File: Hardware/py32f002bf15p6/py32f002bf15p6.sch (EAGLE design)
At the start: 26 parts, among them IC1 PY32F002BF15P6TU, IC2 AP2114HA-3.3TRG1, J1 USB_MINI-B_SMT, Y1 DSC6083CI1A-350K000T

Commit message: Replaced 4.7uf 0805 caps for larger 1206 parts
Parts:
- C10, C9: device rcl:C-EUC0805 -> rcl:C-EUC1206
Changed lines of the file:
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@@
 <part name="GND17" library="supply1" library_urn="urn:adsk.eagle:library:371" deviceset="GND" device=""/>
 <part name="GND19" library="supply1" library_urn="urn:adsk.eagle:library:371" deviceset="GND" device=""/>
-<part name="C9" library="rcl" library_urn="urn:adsk.eagle:library:334" deviceset="C-EU" device="C0805" package3d_urn="urn:adsk.eagle:package:23617/2" value="4.7uf"/>
+<part name="C9" library="rcl" library_urn="urn:adsk.eagle:library:334" deviceset="C-EU" device="C1206" package3d_urn="urn:adsk.eagle:package:23618/2" value="4.7uf"/>
 <part name="GND20" library="supply1" library_urn="urn:adsk.eagle:library:371" deviceset="GND" device=""/>
-<part name="C10" library="rcl" library_urn="urn:adsk.eagle:library:334" deviceset="C-EU" device="C0805" package3d_urn="urn:adsk.eagle:package:23617/2" value="4.7uf"/>
+<part name="C10" library="rcl" library_urn="urn:adsk.eagle:library:334" deviceset="C-EU" device="C1206" package3d_urn="urn:adsk.eagle:package:23618/2" value="4.7uf"/>
 <part name="GND21" library="supply1" library_urn="urn:adsk.eagle:library:371" deviceset="GND" device=""/>
 <part name="+3V9" library="supply1" library_urn="urn:adsk.eagle:library:371" deviceset="+3V3" device=""/>

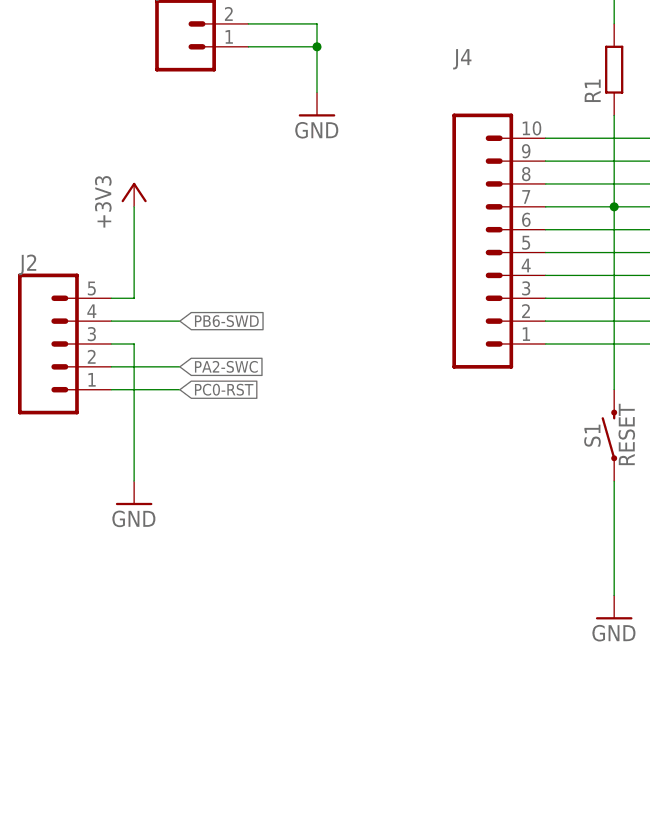
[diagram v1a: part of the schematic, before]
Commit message: Updated silkscreen, removed reset header pin
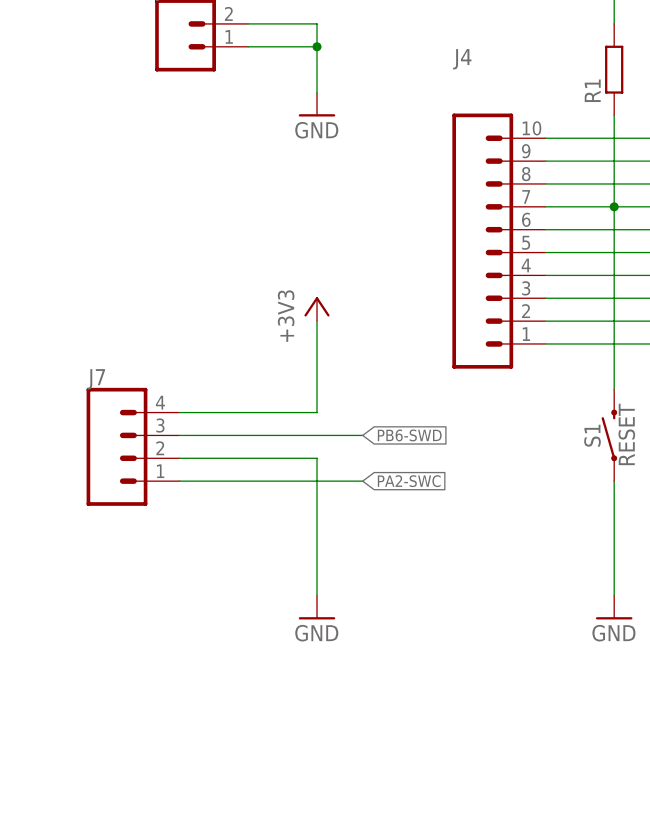
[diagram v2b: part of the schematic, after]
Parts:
- removed J2: (no value), SparkFun-Connectors:CONN_05
- added J7: (no value), SparkFun-Connectors:CONN_04PTH
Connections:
- net +3V3: now also J7.4; no longer J2.5
- net GND: now also J7.2; no longer J2.3
- net PA2-SWC: now also J7.1; no longer J2.2
- net PB6-SWD: now also J7.3; no longer J2.4
- net PC0-RST: no longer J2.1
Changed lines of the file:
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@@
 <part name="+3V9" library="supply1" library_urn="urn:adsk.eagle:library:371" deviceset="+3V3" device=""/>
 <part name="GND4" library="supply1" library_urn="urn:adsk.eagle:library:371" deviceset="GND" device=""/>
-<part name="J2" library="SparkFun-Connectors" deviceset="CONN_05" device=""/>
-<part name="+3V1" library="supply1" library_urn="urn:adsk.eagle:library:371" deviceset="+3V3" device=""/>
-<part name="GND5" library="supply1" library_urn="urn:adsk.eagle:library:371" deviceset="GND" device=""/>
 <part name="JP1" library="SparkFun-Jumpers" deviceset="JUMPER-SMT_2_NC_PASTE" device="_SILK" package3d_urn="urn:adsk.eagle:package:39282/1"/>
 <part name="JP2" library="SparkFun-Jumpers" deviceset="JUMPER-SMT_2_NC_PASTE" device="_SILK" package3d_urn="urn:adsk.eagle:package:39282/1"/>
@@
 <part name="R5" library="rcl" library_urn="urn:adsk.eagle:library:334" deviceset="R-EU_" device="R0805" package3d_urn="urn:adsk.eagle:package:23553/2"/>
 <part name="S3" library="SparkFun-Switches" deviceset="MOMENTARY-SWITCH-SPST" device="-SMD-6.0X3.5MM" value="RESET"/>
+<part name="+3V8" library="supply1" library_urn="urn:adsk.eagle:library:371" deviceset="+3V3" device=""/>
+<part name="GND8" library="supply1" library_urn="urn:adsk.eagle:library:371" deviceset="GND" device=""/>
+<part name="J7" library="SparkFun-Connectors" deviceset="CONN_04" device="PTH"/>
 </parts>
 <sheets>
@@
 <attribute name="VALUE" x="30.48" y="2.54" size="1.778" layer="96"/>
 </instance>
-<instance part="J2" gate="G$1" x="-58.42" y="35.56" smashed="yes">
-<attribute name="VALUE" x="-60.96" y="25.654" size="1.778" layer="96" font="vector"/>
-<attribute name="NAME" x="-60.96" y="43.688" size="1.778" layer="95" font="vector"/>
-</instance>
-<instance part="+3V1" gate="G$1" x="-48.26" y="53.34" smashed="yes">
-<attribute name="VALUE" x="-50.8" y="48.26" size="1.778" layer="96" rot="R90"/>
-</instance>
-<instance part="GND5" gate="1" x="-48.26" y="17.78" smashed="yes">
-<attribute name="VALUE" x="-50.8" y="15.24" size="1.778" layer="96"/>
-</instance>
 <instance part="JP1" gate="G$1" x="223.52" y="25.4" smashed="yes">
 <attribute name="NAME" x="220.98" y="27.94" size="1.778" layer="95" font="vector"/>
@@
 <instance part="S3" gate="G$1" x="114.3" y="20.32" smashed="yes" rot="R90">
 <attribute name="NAME" x="112.776" y="20.32" size="1.778" layer="95" font="vector" rot="R90" align="bottom-center"/>
+</instance>
+<instance part="+3V8" gate="G$1" x="-27.94" y="40.64" smashed="yes">
+<attribute name="VALUE" x="-30.48" y="35.56" size="1.778" layer="96" rot="R90"/>
+</instance>
+<instance part="GND8" gate="1" x="-27.94" y="5.08" smashed="yes">
+<attribute name="VALUE" x="-30.48" y="2.54" size="1.778" layer="96"/>
+</instance>
+<instance part="J7" gate="J1" x="-48.26" y="22.86" smashed="yes">
+<attribute name="VALUE" x="-53.34" y="15.494" size="1.778" layer="96" font="vector"/>
+<attribute name="NAME" x="-53.34" y="30.988" size="1.778" layer="95" font="vector"/>
 </instance>
 </instances>
@@
 </segment>
 <segment>
-<pinref part="J2" gate="G$1" pin="3"/>
-<wire x1="-50.8" y1="35.56" x2="-48.26" y2="35.56" width="0.1524" layer="91"/>
-<wire x1="-48.26" y1="35.56" x2="-48.26" y2="20.32" width="0.1524" layer="91"/>
-<pinref part="GND5" gate="1" pin="GND"/>
-</segment>
-<segment>
 <pinref part="J6" gate="G$1" pin="2"/>
 <wire x1="-35.56" y1="71.12" x2="-27.94" y2="71.12" width="0.1524" layer="91"/>
@@
 <pinref part="Y1" gate="G$1" pin="GND"/>
 </segment>
+<segment>
+<wire x1="-27.94" y1="22.86" x2="-27.94" y2="7.62" width="0.1524" layer="91"/>
+<pinref part="GND8" gate="1" pin="GND"/>
+<pinref part="J7" gate="J1" pin="2"/>
+<wire x1="-43.18" y1="22.86" x2="-27.94" y2="22.86" width="0.1524" layer="91"/>
+</segment>
 </net>
 <net name="PA2-SWC" class="0">
@@
 </segment>
 <segment>
-<pinref part="J2" gate="G$1" pin="2"/>
-<wire x1="-50.8" y1="33.02" x2="-43.18" y2="33.02" width="0.1524" layer="91"/>
-<label x="-43.18" y="33.02" size="1.27" layer="95" xref="yes"/>
+<label x="-22.86" y="20.32" size="1.27" layer="95" xref="yes"/>
+<pinref part="J7" gate="J1" pin="1"/>
+<wire x1="-43.18" y1="20.32" x2="-22.86" y2="20.32" width="0.1524" layer="91"/>
 </segment>
 </net>
@@
 </segment>
 <segment>
-<pinref part="J2" gate="G$1" pin="4"/>
-<wire x1="-50.8" y1="38.1" x2="-43.18" y2="38.1" width="0.1524" layer="91"/>
-<label x="-43.18" y="38.1" size="1.27" layer="95" xref="yes"/>
+<label x="-22.86" y="25.4" size="1.27" layer="95" xref="yes"/>
+<pinref part="J7" gate="J1" pin="3"/>
+<wire x1="-43.18" y1="25.4" x2="-22.86" y2="25.4" width="0.1524" layer="91"/>
 </segment>
 </net>
@@
 <wire x1="5.08" y1="50.8" x2="5.08" y2="60.96" width="0.1524" layer="91"/>
 </segment>
-<segment>
-<pinref part="J2" gate="G$1" pin="1"/>
-<wire x1="-50.8" y1="30.48" x2="-43.18" y2="30.48" width="0.1524" layer="91"/>
-<label x="-43.18" y="30.48" size="1.27" layer="95" xref="yes"/>
-</segment>
 </net>
 <net name="N$6" class="1">
@@
 </segment>
 <segment>
-<pinref part="J2" gate="G$1" pin="5"/>
-<wire x1="-50.8" y1="40.64" x2="-48.26" y2="40.64" width="0.1524" layer="91"/>
-<wire x1="-48.26" y1="40.64" x2="-48.26" y2="50.8" width="0.1524" layer="91"/>
-<pinref part="+3V1" gate="G$1" pin="+3V3"/>
-</segment>
-<segment>
 <pinref part="J5" gate="G$1" pin="1"/>
 <wire x1="-35.56" y1="81.28" x2="-27.94" y2="81.28" width="0.1524" layer="91"/>
@@
 <wire x1="27.94" y1="83.82" x2="27.94" y2="88.9" width="0.1524" layer="91"/>
 </segment>
-</net>
+<segment>
+<wire x1="-27.94" y1="27.94" x2="-27.94" y2="38.1" width="0.1524" layer="91"/>
+<pinref part="+3V8" gate="G$1" pin="+3V3"/>
+<pinref part="J7" gate="J1" pin="4"/>
+<wire x1="-43.18" y1="27.94" x2="-27.94" y2="27.94" width="0.1524" layer="91"/>
+</segment>
+</net>
